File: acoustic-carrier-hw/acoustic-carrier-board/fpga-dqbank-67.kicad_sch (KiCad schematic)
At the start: 41 parts, among them IC1 ECP5-BGA256, Y601 Crystal Oscillator

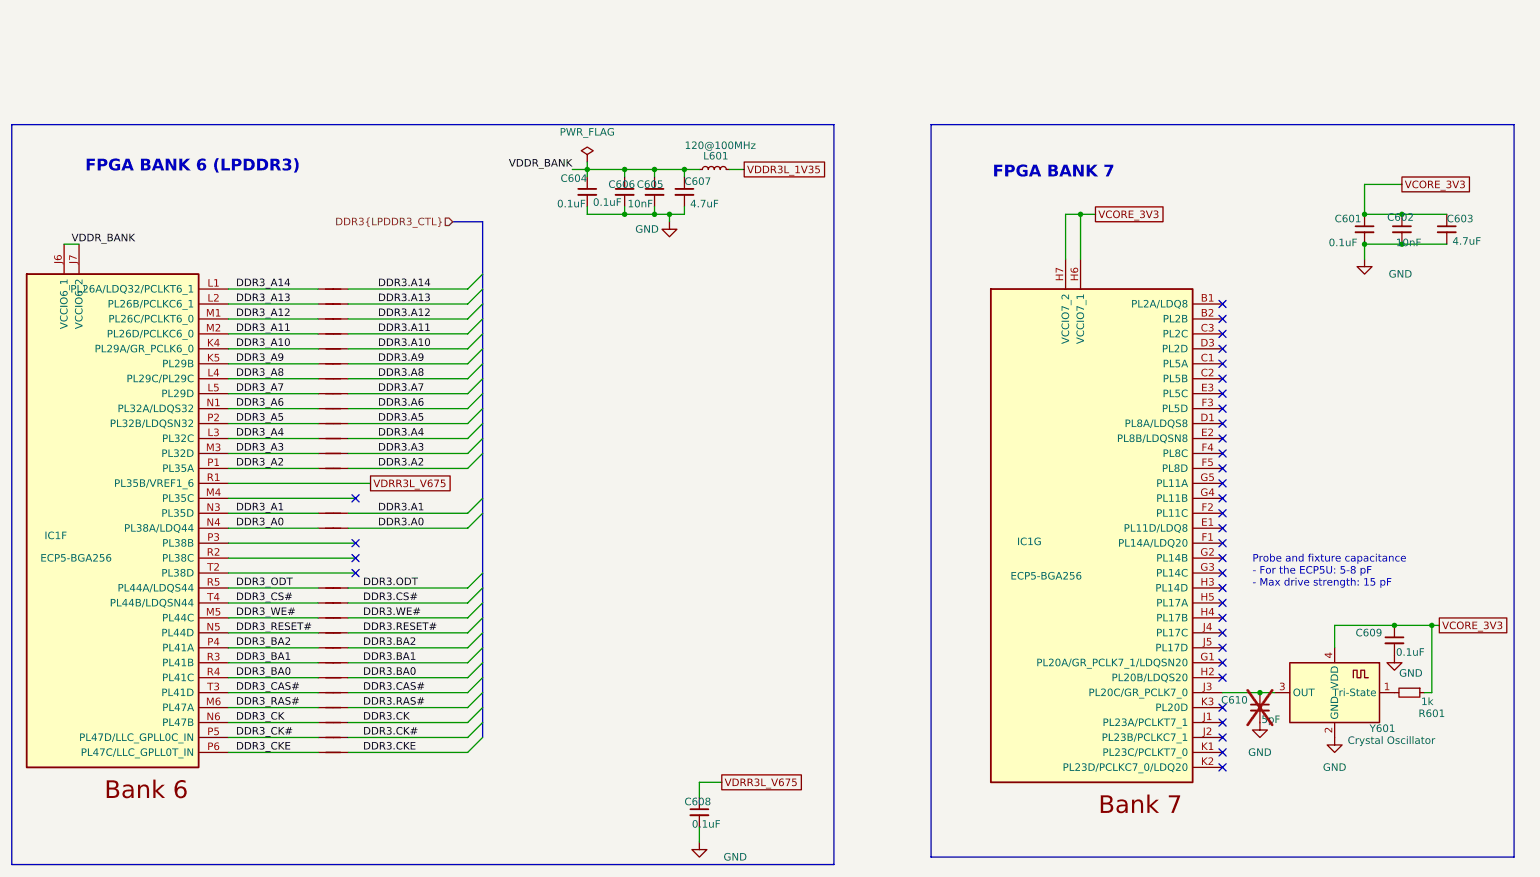
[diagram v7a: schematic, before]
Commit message: [carrier] Removed USB-switch, placed decouplpling for DDR3 and ECP5U (next) consider adding buffers on CC1 and CC2 pins
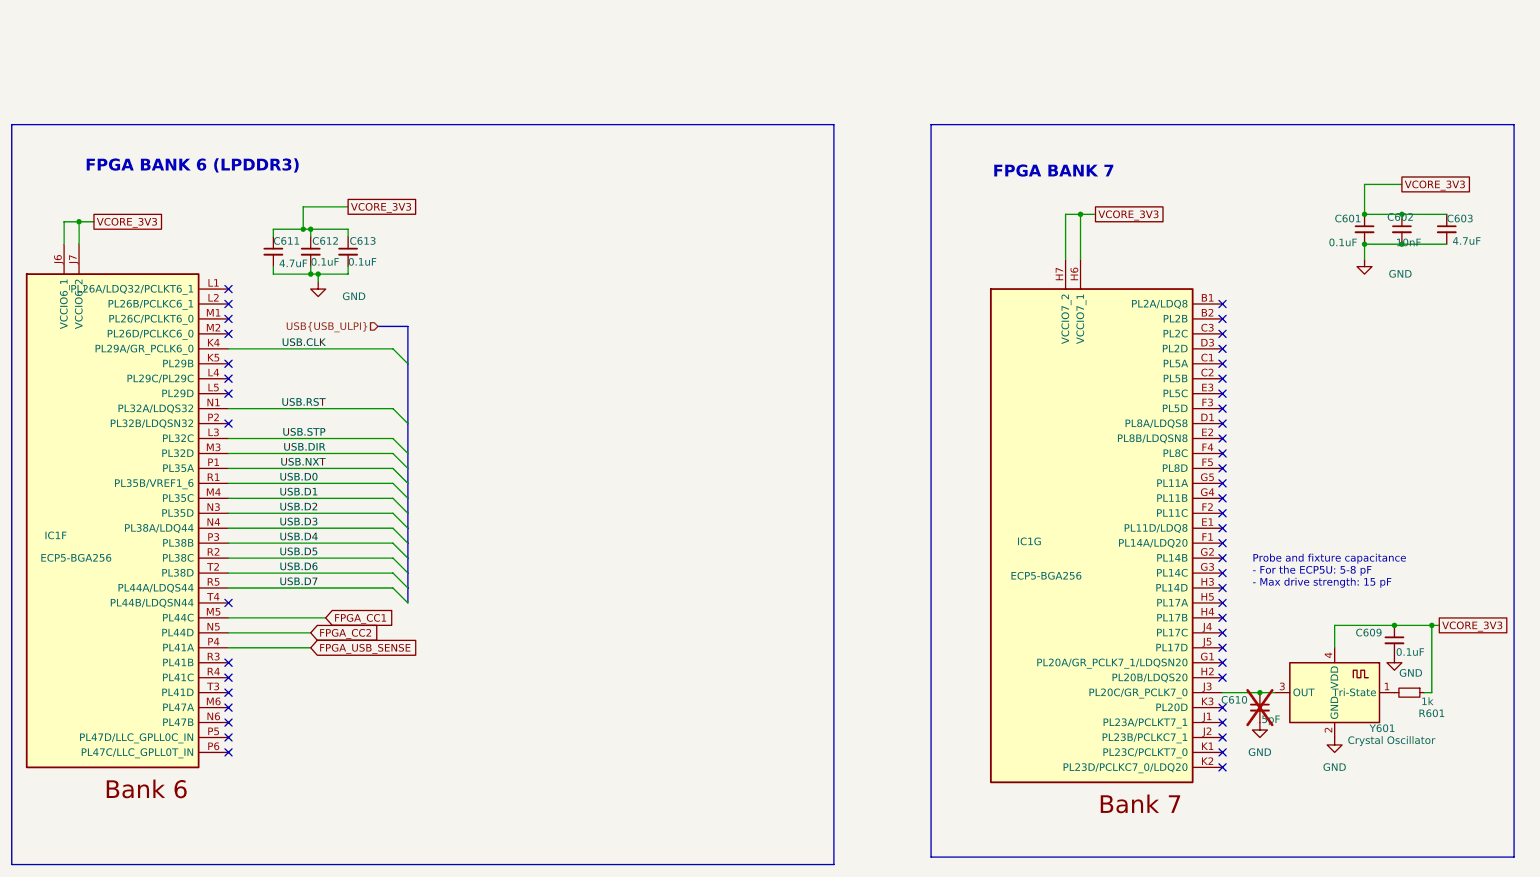
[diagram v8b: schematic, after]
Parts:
- removed C604, C605, C608: 0.1uF, Capacitor_SMD:C_0402_1005Metric, symbol Device:C_Small
- removed C606: 10nF, Capacitor_SMD:C_0402_1005Metric, symbol Device:C_Small
- removed C607: 4.7uF, Capacitor_SMD:C_0402_1005Metric, symbol Device:C_Small
- removed L601: 120@100MHz, Inductor_SMD:L_0603_1608Metric, symbol Device:L_Small
- removed NT601, NT602, NT603, NT604, NT605, NT606, NT607, NT608, NT609, NT610, NT613, NT614, NT615, NT616, NT617, NT618, NT619, NT620, NT621, NT622, NT623, NT624, NT625, NT626, NT627: NetTie_2, iw-misc:NetTie-2_SMD_Pad0.1565mm, symbol Device:NetTie_2
- removed NT611, NT612: NetTie_2, iw-misc:NetTie-2_SMD_Pad0.1240mm, symbol Device:NetTie_2
- added C611: 4.7uF, Capacitor_SMD:C_0402_1005Metric, symbol Device:C_Small
- added C612, C613: 0.1uF, Capacitor_SMD:C_0201_0603Metric, symbol Device:C_Small
- C601, C609: footprint Capacitor_SMD:C_0402_1005Metric -> Capacitor_SMD:C_0201_0603Metric; LPN C307331 -> C22435929; MPN CL05B104KB54PNC -> CGA0201X7R104K160ET
- C602: footprint Capacitor_SMD:C_0402_1005Metric -> Capacitor_SMD:C_0201_0603Metric; LPN C15195 -> C285010; MPN CL05B103KB5NNNC -> 0201B103K250NT
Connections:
- net VDDR_BANK is gone; now on net VCORE_3V3: IC1.J6 (VCCIO6_1), IC1.J7 (VCCIO6_2)
- net GND: now also C611.2, C612.2, C613.2
- net VCORE_3V3: now also C611.1, C612.1, C613.1
- net USB.D1: now reaches IC1.M4 (PL35C)
- net USB.D4: now reaches IC1.P3 (PL38B)
- net USB.D5: now reaches IC1.R2 (PL38C)
- net USB.D6: now reaches IC1.T2 (PL38D)
- net DDR3_A0 renamed USB.D3
- net DDR3_A1 renamed USB.D2
- net DDR3_A10 renamed USB.CLK
- net DDR3_A11: no longer names the net of IC1.M2 (PL26D/PCLKC6_0)
- net DDR3_A12: no longer names the net of IC1.M1 (PL26C/PCLKT6_0)
- net DDR3_A13: no longer names the net of IC1.L2 (PL26B/PCLKC6_1)
- net DDR3_A14: no longer names the net of IC1.L1 (PL26A/LDQ32/PCLKT6_1)
- net DDR3_A2 renamed USB.NXT
- net DDR3_A3 renamed USB.DIR
- net DDR3_A4 renamed USB.STP
- net DDR3_A5: no longer names the net of IC1.P2 (PL32B/LDQSN32)
- net DDR3_A6 renamed USB.RST
- net DDR3_A7: no longer names the net of IC1.L5 (PL29D)
- net DDR3_A8: no longer names the net of IC1.L4 (PL29C/PL29C)
- net DDR3_A9: no longer names the net of IC1.K5 (PL29B)
- net DDR3_BA0: no longer names the net of IC1.R4 (PL41C)
- net DDR3_BA1: no longer names the net of IC1.R3 (PL41B)
- net DDR3_BA2 renamed FPGA_USB_SENSE
- net DDR3_CAS#: no longer names the net of IC1.T3 (PL41D)
- net DDR3_CK: no longer names the net of IC1.N6 (PL47B)
- net DDR3_CK#: no longer names the net of IC1.P5 (PL47D/LLC_GPLL0C_IN)
- net DDR3_CKE: no longer names the net of IC1.P6 (PL47C/LLC_GPLL0T_IN)
- net DDR3_CS#: no longer names the net of IC1.T4 (PL44B/LDQSN44)
- net DDR3_ODT renamed USB.D7
- net DDR3_RAS#: no longer names the net of IC1.M6 (PL47A)
- net DDR3_RESET# renamed FPGA_CC2
- net DDR3_WE# renamed FPGA_CC1
- net VDRR3L_V675 renamed USB.D0
- no-connect marks 35 -> 47
